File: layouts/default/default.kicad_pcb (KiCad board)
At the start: 2 copper layers, 77 parts

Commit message: documentation
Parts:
- added R37: , YAGEO_RC0805FR_071KL:R0805, F.Cu at (0.00, -30.0)
- added R38: , YAGEO_RC0805FR_07100RL:R0805, F.Cu at (0.00, -10.0)
- added R39: , FOJAN_FRC0805F1003TS:R0805, F.Cu at (0.00, -20.0)
- added U1: , Sharp_Microelectronics_PC817X2CSP9F:SMD-4_L4.6-W6.5-P2.54-LS10.2-TL, F.Cu at (0.00, 0.00)
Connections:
- CN1 pad 4: footprint-R-0 -> footprint-R-1
- CN2 pad 4: footprint-R-1 -> footprint-R-0

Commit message: dont even know whats up w the max current thing
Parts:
- added C1: , YAGEO_CC0805KRX7R9BB104:C0805, F.Cu at (0.00, 0.00)
- added C2: , Samsung_Electro_Mechanics_CL31A107MQHNNNE:C1206, F.Cu at (0.00, -10.0)
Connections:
- net footprint-R-0 renamed R
- CN1 pad 4: footprint-R-1 -> GND

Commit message: vibe coded garbage to try to get the pcb to not have duplicate refdes
at least a rough draft of the pcb is done tho

the current workflow is
delete everything on pcb, save, ato build, uv run old.py, open kicad, then manually delete the extras, and move the remaining refdes and layout route as normal.
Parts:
- R1: footprint YAGEO_RC0805FR_07120RL:R0805 -> YAGEO_RC0805FR_071KL:R0805
- R2: footprint YAGEO_RC0805FR_07120RL:R0805 -> YAGEO_RC0805FR_07100RL:R0805
- R3: footprint YAGEO_RC0805FR_07120RL:R0805 -> FOJAN_FRC0805F1003TS:R0805
- R37: footprint YAGEO_RC0805FR_071KL:R0805 -> YAGEO_RC0805FR_07120RL:R0805
- R38: footprint YAGEO_RC0805FR_07100RL:R0805 -> YAGEO_RC0805FR_07120RL:R0805
- R39: footprint FOJAN_FRC0805F1003TS:R0805 -> YAGEO_RC0805FR_07120RL:R0805
- moved R10 350.1 mm to (3.86, 42.7)
- moved LED7 315.4 mm to (7.47, 42.7), turned to 180 degrees
- moved LED8 305.5 mm to (27.5, 42.7), turned to 180 degrees
- moved LED9 295.6 mm to (47.5, 42.7), turned to 180 degrees
- moved R34 288.5 mm to (3.86, 122.7)
- moved R4 288.0 mm to (3.86, 22.7)
- moved LED10 285.7 mm to (67.5, 42.7), turned to 180 degrees
- moved R35 279.6 mm to (23.9, 122.7)
- moved R5 278.1 mm to (23.9, 22.7)
- moved R36 270.9 mm to (43.9, 122.7)
- moved R6 268.1 mm to (43.9, 22.7)
- moved R7 258.2 mm to (63.9, 22.7)
- moved LED31 254.1 mm to (7.47, 122.7), turned to 180 degrees
- moved R8 248.3 mm to (83.9, 22.7)
- moved LED32 245.4 mm to (27.5, 122.7), turned to 180 degrees
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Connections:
- R1 pad 1: VCC -> footprint-T-1
- R1 pad 2: footprint-A-0 -> _1
- R10 pad 2: footprint-A-35 -> footprint-A-32
- R11 pad 2: footprint-A-1 -> footprint-A-33
- R12 pad 2: footprint-A-2 -> footprint-A-34
- R13 pad 2: footprint-A-3 -> footprint-A-35
- R14 pad 2: footprint-A-4 -> footprint-A-1
- R15 pad 2: footprint-A-5 -> footprint-A-2
- R16 pad 2: footprint-A-6 -> footprint-A-3
- R17 pad 2: footprint-A-7 -> footprint-A-4
- R18 pad 2: footprint-A-8 -> footprint-A-5
- R19 pad 2: footprint-A-9 -> footprint-A-6
- R2 pad 1: VCC -> R
- R2 pad 2: footprint-A-11 -> G
- R20 pad 2: footprint-A-10 -> footprint-A-7
- R21 pad 2: footprint-A-12 -> footprint-A-8
- R22 pad 2: footprint-A-13 -> footprint-A-9
- R23 pad 2: footprint-A-14 -> footprint-A-10
- R24 pad 2: footprint-A-15 -> footprint-A-12
- R25 pad 2: footprint-A-16 -> footprint-A-13
- R26 pad 2: footprint-A-17 -> footprint-A-14
- R27 pad 2: footprint-A-18 -> footprint-A-15
- R28 pad 2: footprint-A-19 -> footprint-A-16
- R29 pad 2: footprint-A-20 -> footprint-A-17
- R3 pad 1: VCC -> G
- R3 pad 2: footprint-A-22 -> GND
- R30 pad 2: footprint-A-21 -> footprint-A-18
- R31 pad 2: footprint-A-23 -> footprint-A-19
- R32 pad 2: footprint-A-24 -> footprint-A-20
- R33 pad 2: footprint-A-25 -> footprint-A-21
- R34 pad 2: footprint-A-26 -> footprint-A-23
- R35 pad 2: footprint-A-27 -> footprint-A-24
- R36 pad 2: footprint-A-28 -> footprint-A-25
- R37 pad 1: footprint-T-1 -> VCC
- R37 pad 2: _1 -> footprint-A-26
- R38 pad 1: R -> VCC
- R38 pad 2: G -> footprint-A-27
- R39 pad 1: G -> VCC
- R39 pad 2: GND -> footprint-A-28
- R4 pad 2: footprint-A-29 -> footprint-A-0
- R5 pad 2: footprint-A-30 -> footprint-A-11
- R6 pad 2: footprint-A-31 -> footprint-A-22
- R7 pad 2: footprint-A-32 -> footprint-A-29
- R8 pad 2: footprint-A-33 -> footprint-A-30
- R9 pad 2: footprint-A-34 -> footprint-A-31
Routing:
- net VCC: track 0.00 -> 824.1 mm
- net K: track 0.00 -> 798.3 mm, vias 0 -> 2
- net GND: track 0.00 -> 19.9 mm
- net footprint-A-8: track 0.00 -> 1.81 mm
- net footprint-A-7: track 0.00 -> 1.81 mm
- net footprint-A-6: track 0.00 -> 1.81 mm
- net footprint-A-5: track 0.00 -> 1.81 mm
- net footprint-A-4: track 0.00 -> 1.81 mm
- net footprint-A-35: track 0.00 -> 1.81 mm
- net footprint-A-34: track 0.00 -> 1.81 mm
- net footprint-A-33: track 0.00 -> 1.81 mm
- net footprint-A-31: track 0.00 -> 1.81 mm
- net footprint-A-30: track 0.00 -> 1.81 mm
- net footprint-A-29: track 0.00 -> 1.81 mm
- net footprint-A-28: track 0.00 -> 1.81 mm
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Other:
- board outline added: 110 x 130 mm

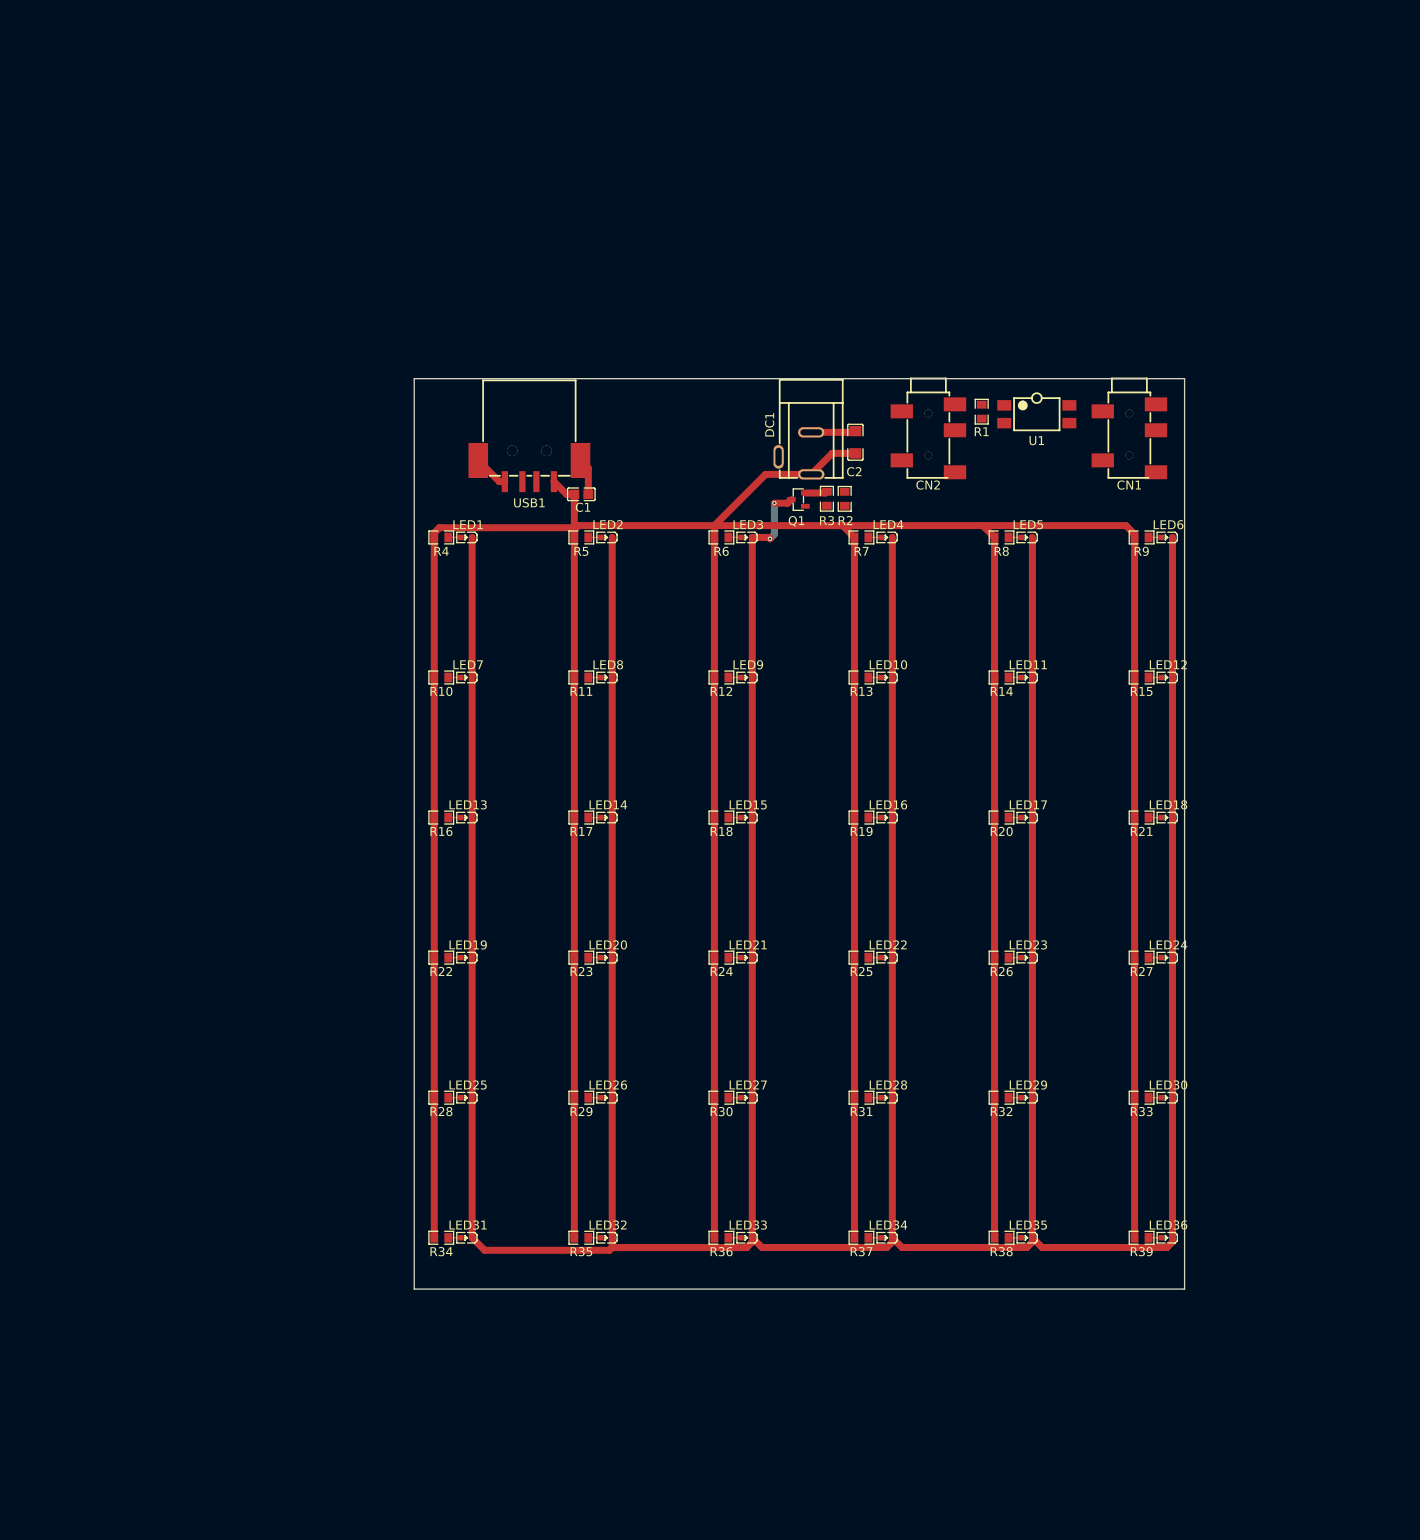
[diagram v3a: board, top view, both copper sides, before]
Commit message: gerbers, mounting holes, gnd and vcc fills
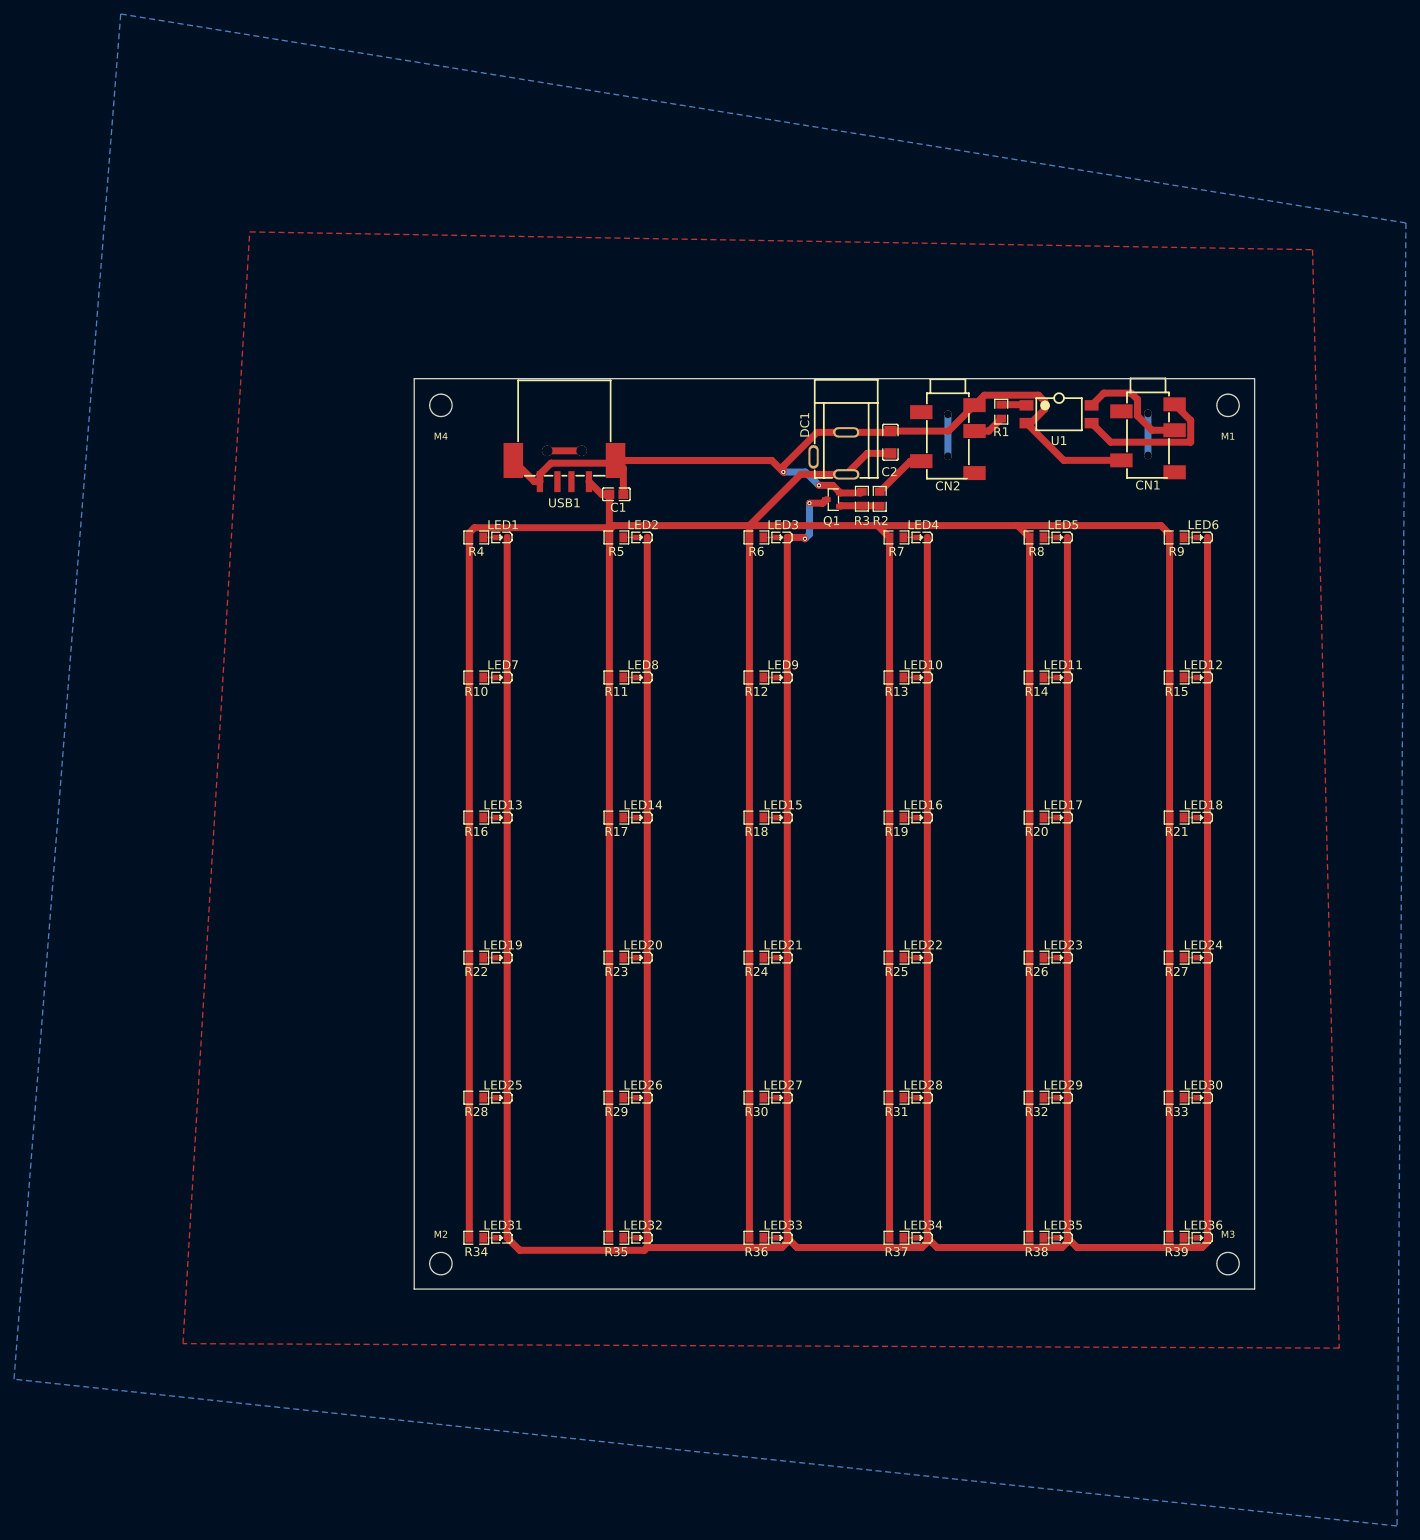
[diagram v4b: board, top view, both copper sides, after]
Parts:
- added M1: MountingHole_3.2mm_M3, MountingHole:MountingHole_3.2mm_M3, F.Cu at (116.2, 3.81)
- added M2: MountingHole_3.2mm_M3, MountingHole:MountingHole_3.2mm_M3, F.Cu at (3.81, 126.4)
- added M3: MountingHole_3.2mm_M3, MountingHole:MountingHole_3.2mm_M3, F.Cu at (116.2, 126.4)
- added M4: MountingHole_3.2mm_M3, MountingHole:MountingHole_3.2mm_M3, F.Cu at (3.81, 3.81)
- moved C2 5.00 mm to (68.0, 9.08)
- moved LED1 5.00 mm to (12.5, 22.7)
- moved LED13 5.00 mm to (12.5, 62.7)
- moved LED19 5.00 mm to (12.5, 82.7)
- moved LED25 5.00 mm to (12.5, 102.7)
- moved LED31 5.00 mm to (12.5, 122.7)
- moved LED7 5.00 mm to (12.5, 42.7)
- moved C1 5.00 mm to (28.9, 16.5)
- moved DC1 5.00 mm to (59.4, 10.7)
- moved LED10 5.00 mm to (72.5, 42.7)
- moved LED11 5.00 mm to (92.5, 42.7)
- moved LED12 5.00 mm to (112.5, 42.7)
- moved LED14 5.00 mm to (32.5, 62.7)
- moved LED15 5.00 mm to (52.5, 62.7)
- moved LED16 5.00 mm to (72.5, 62.7)
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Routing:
- net GND: track 19.9 -> 123.2 mm, vias 0 -> 2
- net S: track 0.00 -> 21.6 mm
- net footprint-T-0: track 0.00 -> 16.1 mm
- net R: track 0.00 -> 7.75 mm
- net footprint-net-1: track 0.00 -> 6.00 mm
- net footprint-net-0: track 0.00 -> 6.00 mm
- net G: track 0.00 -> 5.66 mm
- net footprint-net-2: track 0.00 -> 4.90 mm
- net footprint-T-1: track 0.00 -> 4.55 mm
- net _1: track 0.20 -> 3.64 mm
- added copper zone on B.Cu, net GND
- added copper zone on F.Cu, net VCC
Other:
- board size 110 x 130 mm -> 120 x 130 mm

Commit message: besides mounting holes, the pcb is almost there
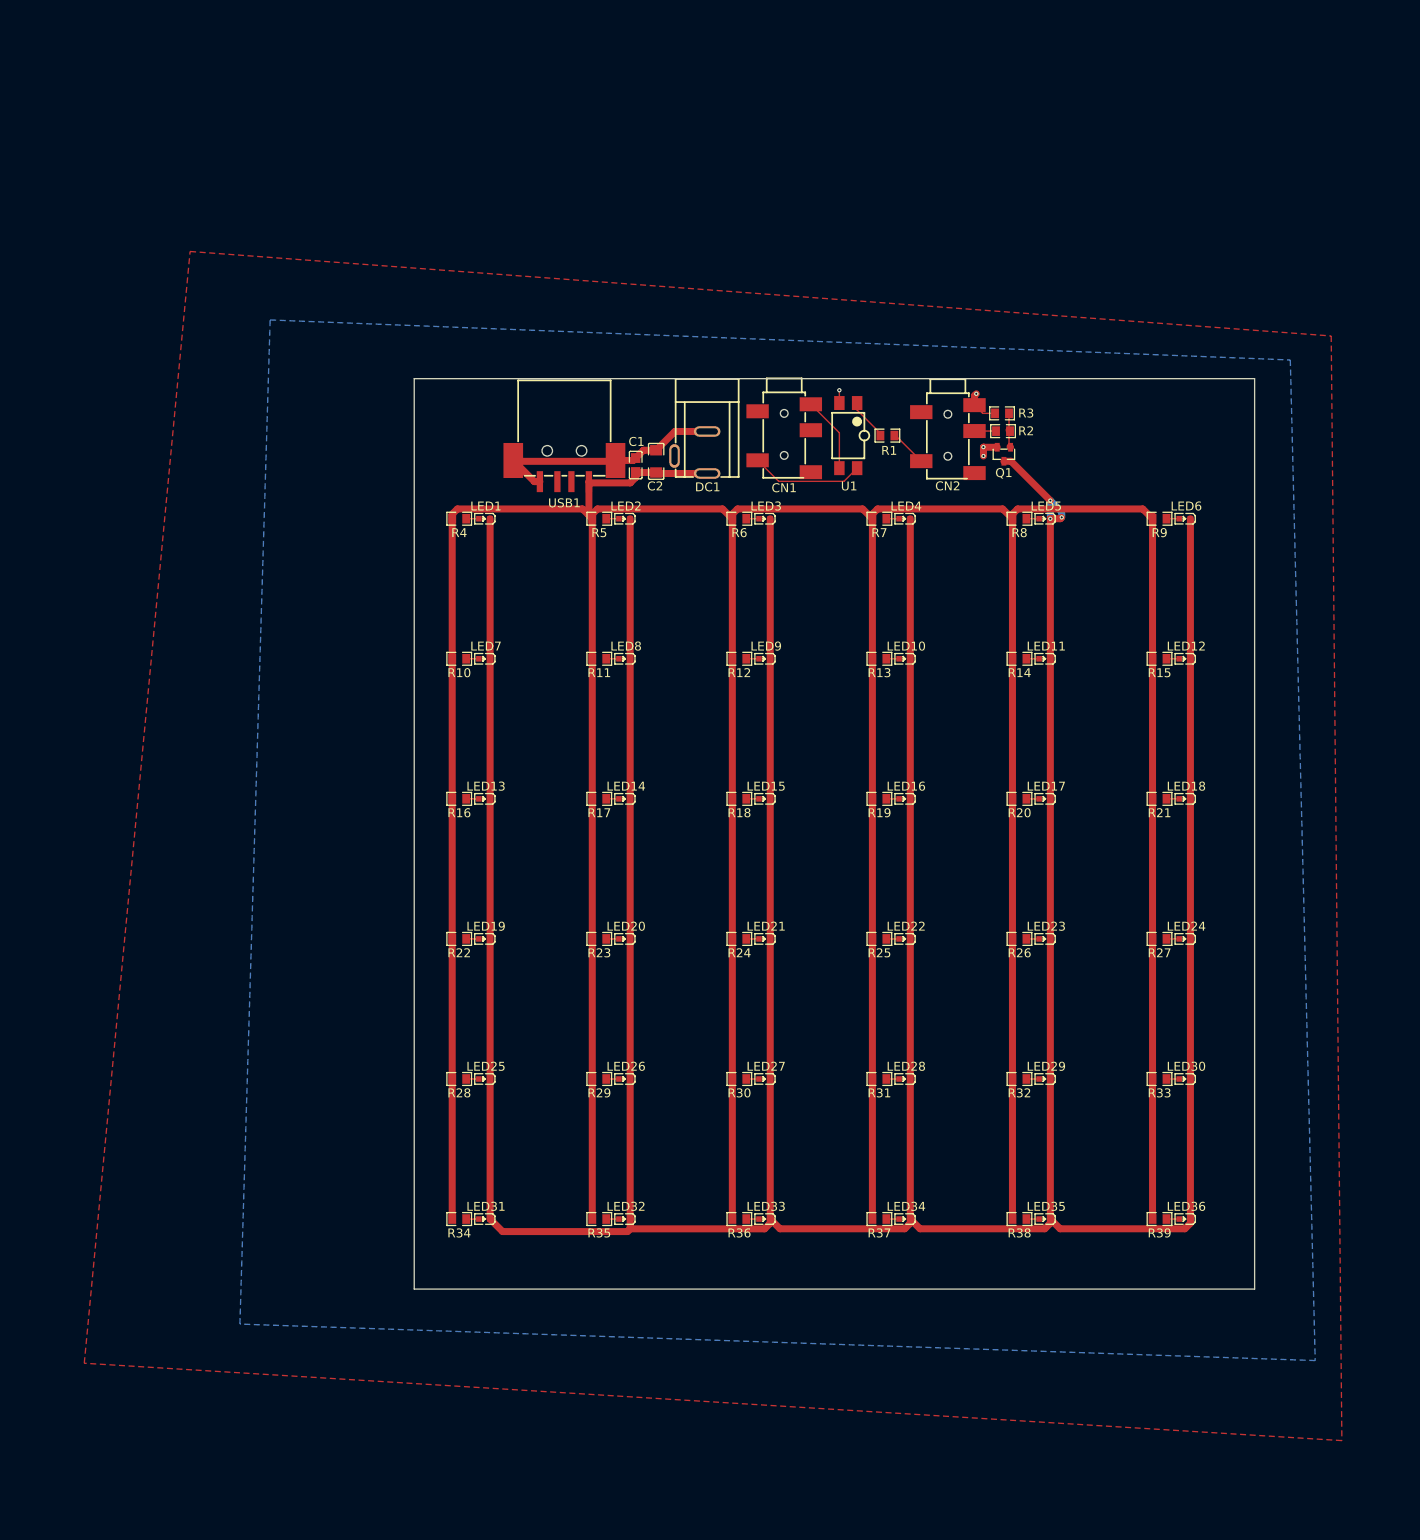
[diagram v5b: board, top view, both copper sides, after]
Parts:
- removed M1, M2, M3, M4: MountingHole_3.2mm_M3, MountingHole:MountingHole_3.2mm_M3
- moved CN1 51.9 mm to (52.8, 8.51)
- moved C2 33.6 mm to (34.5, 11.8)
- moved U1 30.3 mm to (62.0, 8.13), turned to -90 degrees
- moved Q1 25.2 mm to (84.2, 10.8), turned to 90 degrees
- moved R3 23.4 mm to (83.9, 4.95), turned to 180 degrees
- moved R2 20.1 mm to (84.1, 7.49), turned to 0 degrees
- moved DC1 19.9 mm to (39.5, 10.5)
- moved R1 16.6 mm to (67.6, 8.13), turned to 180 degrees
- moved C1 5.01 mm to (31.6, 12.3), turned to 90 degrees
- moved LED1 3.62 mm to (10.0, 20.0)
- moved LED2 3.62 mm to (30.0, 20.0)
- moved LED3 3.62 mm to (50.0, 20.0)
- moved LED4 3.62 mm to (70.0, 20.0)
- moved LED5 3.62 mm to (90.0, 20.0)
- moved LED6 3.62 mm to (110.0, 20.0)
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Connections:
- CN1 pad : footprint-net-0 -> (no net)
- CN1 pad 3: footprint-T-0 -> footprint-R-1
- CN1 pad 4: GND -> footprint-T-0
- CN2 pad : footprint-net-1 -> (no net)
- CN2 pad 3: footprint-T-1 -> footprint-R-0
- CN2 pad 4: R -> footprint-T-1
- R2 pad 1: R -> footprint-R-0
- USB1 pad : footprint-net-2 -> (no net)
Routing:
- net GND: track 123.2 -> 45.5 mm, vias 2 -> 4
- net VCC: track 824.1 -> 811.8 mm
- net S: track 21.6 -> 10.8 mm
- net R: track 7.75 -> 0.00 mm
- net footprint-net-1: track 6.00 -> 0.00 mm
- net footprint-net-0: track 6.00 -> 0.00 mm
- net K: track 798.3 -> 804.1 mm, vias 2 -> 3
- net footprint-net-2: track 4.90 -> 0.00 mm
- net footprint-R-0: track 0.00 -> 3.08 mm
- net _1: track 3.64 -> 6.02 mm
- net footprint-T-1: track 4.55 -> 5.35 mm
